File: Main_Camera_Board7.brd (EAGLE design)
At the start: 127 x 50.8 mm, 8 parts

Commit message: put leds in correct positions
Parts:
- moved U$3 15.2 mm to (111.8, 29.2)
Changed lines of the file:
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@@
 <?xml version="1.0" encoding="utf-8"?>
 <!DOCTYPE eagle SYSTEM "eagle.dtd">
-<eagle version="7.6.0">
+<eagle version="7.7.0">
 <drawing>
 <settings>
@@
 <setting verticaltext="up"/>
 </settings>
-<grid distance="0.05" unitdist="mm" unit="mm" style="lines" multiple="1" display="yes" altdistance="0.025" altunitdist="inch" altunit="inch"/>
+<grid distance="0.01" unitdist="inch" unit="inch" style="lines" multiple="1" display="yes" altdistance="0.025" altunitdist="inch" altunit="inch"/>
 <layers>
 <layer number="1" name="Top" color="4" fill="1" visible="yes" active="yes"/>
@@
 <element name="U$1" library="camera" package="ELP-USBFHD01M-L21" value="ELP-USBFHD01M-L21" x="58.42" y="25.4"/>
 <element name="U$2" library="camera" package="LED" value="LED" x="10.16" y="29.21"/>
-<element name="U$3" library="camera" package="LED" value="LED" x="96.52" y="29.21"/>
+<element name="U$3" library="camera" package="LED" value="LED" x="111.76" y="29.16"/>
 <element name="U$4" library="camera" package="T2I" value="T21" x="1.75" y="44.45" rot="R270"/>
 <element name="U$5" library="camera" package="T2I" value="T21" x="1.75" y="25.4" rot="R270"/>
@@
 <contactref element="U$3" pad="P$3"/>
 <contactref element="U$3" pad="P$1"/>
-<wire x1="96.52" y1="29.21" x2="97.67" y2="29.21" width="0" layer="19" extent="1-1"/>
-<wire x1="11.31" y1="29.21" x2="96.52" y2="29.21" width="0" layer="19" extent="1-1"/>
+<wire x1="111.76" y1="29.16" x2="112.91" y2="29.16" width="0" layer="19" extent="1-1"/>
+<wire x1="11.31" y1="29.21" x2="111.76" y2="29.16" width="0" layer="19" extent="1-1"/>
 <wire x1="10.16" y1="29.21" x2="11.31" y2="29.21" width="0" layer="19" extent="1-1"/>
 <wire x1="1.75" y1="37.05" x2="10.16" y2="29.21" width="0" layer="19" extent="1-1"/>

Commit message: more updates
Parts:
- moved SERVO 77.4 mm to (95.7, 3.08)
- moved U$3 15.2 mm to (96.5, 29.2)
- flipped LIGHT1 to the bottom
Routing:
- net PWN: track 0.00 -> 113.2 mm
- net +5VCAMERA: track 14.0 -> 110.5 mm
- net +3.3V: track 137.9 -> 50.2 mm
- net N$8: track 0.00 -> 86.2 mm
- net N$5: track 57.8 -> 0.00 mm
- net N$1: track 43.3 -> 0.00 mm
- net N$6: track 10.8 -> 0.00 mm
- net D_P: track 60.6 -> 58.9 mm
- net D_M: track 63.7 -> 62.6 mm

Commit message: Added TODO list
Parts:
- moved U$3 14.5 mm to (111.0, 29.2)
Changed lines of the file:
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@@
 <?xml version="1.0" encoding="utf-8"?>
 <!DOCTYPE eagle SYSTEM "eagle.dtd">
-<eagle version="7.6.0">
+<eagle version="7.7.0">
 <drawing>
 <settings>
@@
 <setting verticaltext="up"/>
 </settings>
-<grid distance="0.05" unitdist="mm" unit="mm" style="lines" multiple="1" display="yes" altdistance="0.025" altunitdist="inch" altunit="inch"/>
+<grid distance="0.01" unitdist="inch" unit="inch" style="lines" multiple="1" display="yes" altdistance="0.025" altunitdist="inch" altunit="inch"/>
 <layers>
 <layer number="1" name="Top" color="4" fill="1" visible="yes" active="yes"/>
@@
 <element name="U$1" library="camera" package="ELP-USBFHD01M-L21" value="ELP-USBFHD01M-L21" x="58.42" y="25.4"/>
 <element name="U$2" library="camera" package="LED" value="LED" x="10.16" y="29.21"/>
-<element name="U$3" library="camera" package="LED" value="LED" x="96.52" y="29.21"/>
+<element name="U$3" library="camera" package="LED" value="LED" x="110.998" y="29.21"/>
 <element name="U$4" library="camera" package="T2I" value="T21" x="1.75" y="44.45" rot="R270"/>
 <element name="U$5" library="camera" package="T2I" value="T21" x="1.75" y="25.4" rot="R270"/>
@@
 <contactref element="U$3" pad="P$3"/>
 <contactref element="U$3" pad="P$1"/>
-<wire x1="96.52" y1="29.21" x2="97.67" y2="29.21" width="0" layer="19" extent="1-1"/>
-<wire x1="11.31" y1="29.21" x2="96.52" y2="29.21" width="0" layer="19" extent="1-1"/>
+<wire x1="110.998" y1="29.21" x2="112.148" y2="29.21" width="0" layer="19" extent="1-1"/>
+<wire x1="11.31" y1="29.21" x2="110.998" y2="29.21" width="0" layer="19" extent="1-1"/>
 <wire x1="10.16" y1="29.21" x2="11.31" y2="29.21" width="0" layer="19" extent="1-1"/>
 <wire x1="1.75" y1="37.05" x2="10.16" y2="29.21" width="0" layer="19" extent="1-1"/>

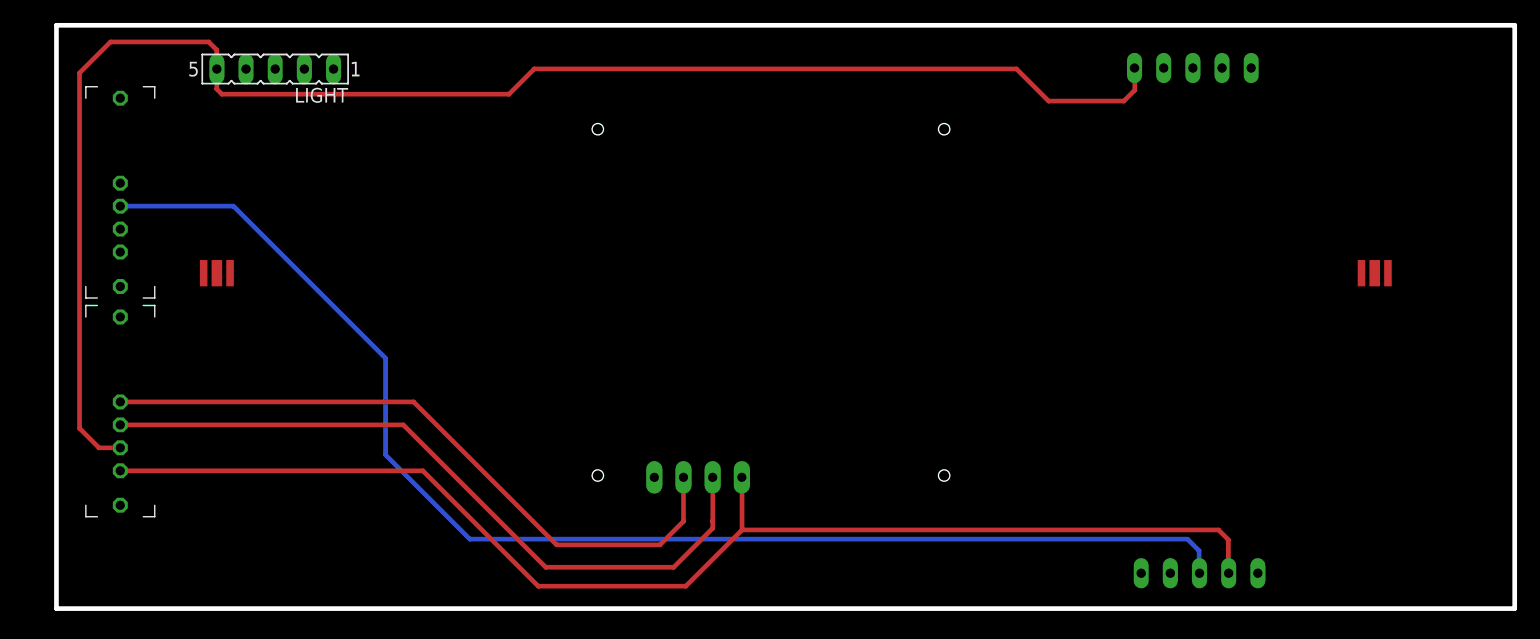
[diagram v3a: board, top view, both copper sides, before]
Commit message: made a few changes to camera board
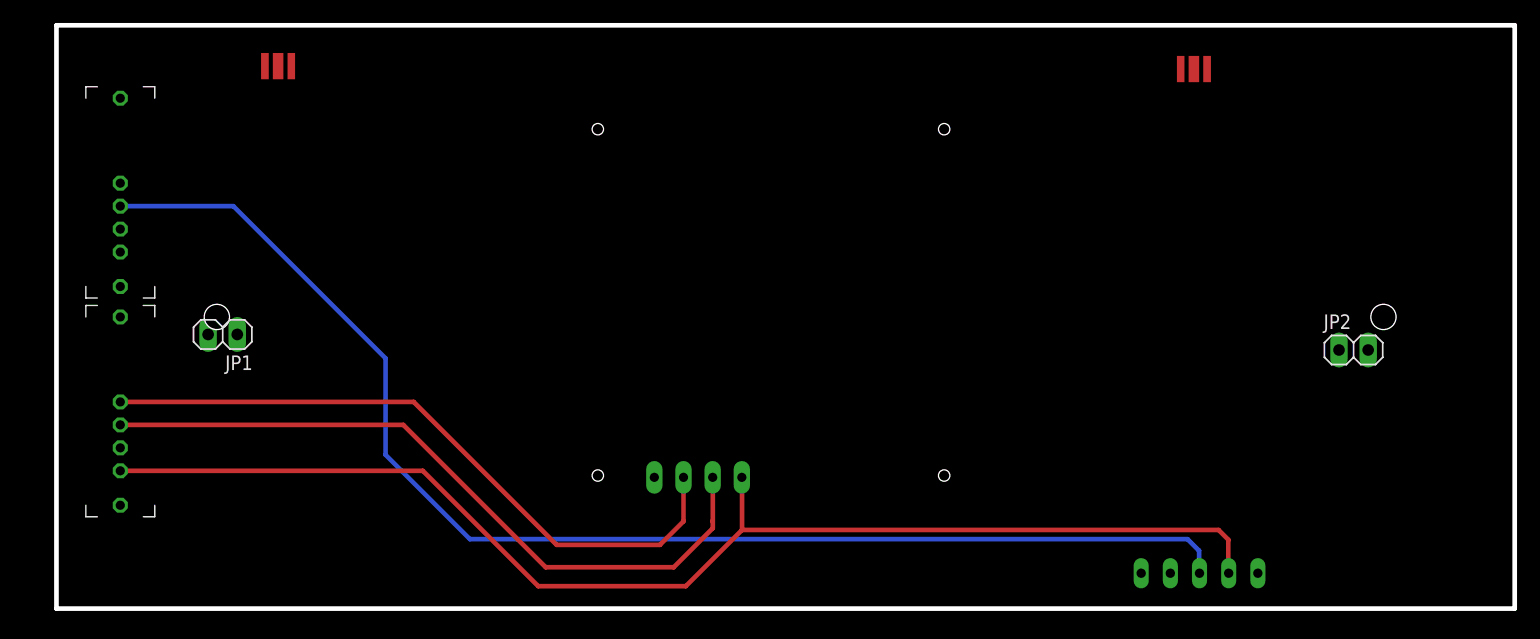
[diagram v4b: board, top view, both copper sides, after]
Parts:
- removed LIGHT, LIGHT1: (no value), con-lsta:FE05-1
- added JP1, JP2: (no value), pinhead:1X02
- moved U$3 23.8 mm to (95.2, 47.0)
- moved U$2 18.8 mm to (15.5, 47.2)
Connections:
- net +3.3V: no longer LIGHT.5, LIGHT1.5
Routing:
- net N$8: track 86.2 -> 0.00 mm
- net +3.3V: track 50.2 -> 0.00 mm
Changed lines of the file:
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@@
 <layers>
 <layer number="1" name="Top" color="4" fill="1" visible="yes" active="yes"/>
+<layer number="2" name="Route2" color="1" fill="3" visible="no" active="no"/>
+<layer number="3" name="Route3" color="4" fill="3" visible="no" active="no"/>
+<layer number="14" name="Route14" color="1" fill="6" visible="no" active="no"/>
+<layer number="15" name="Route15" color="4" fill="6" visible="no" active="no"/>
 <layer number="16" name="Bottom" color="1" fill="1" visible="yes" active="yes"/>
 <layer number="17" name="Pads" color="2" fill="1" visible="yes" active="yes"/>
@@
 <wire x1="109.22" y1="31.75" x2="109.22" y2="26.67" width="0.4064" layer="51"/>
 <text x="-5.08" y="53.34" size="1.778" layer="51">5 in x 2 in</text>
+<hole x="10.16" y="25.4" drill="2.2"/>
+<hole x="111.76" y="25.4" drill="2.2"/>
 </plain>
 <attributes>
@@
 <attribute name="OC_NEWARK" value="unknown" x="95.74" y="3.08" size="1.778" layer="28" rot="MR0" display="off"/>
 </element>
-<element name="LIGHT" library="con-lsta" package="FE05-1" value="" x="15.24" y="46.99" rot="R180">
-<attribute name="MF" value="" x="15.24" y="46.99" size="1.778" layer="27" rot="R180" display="off"/>
-<attribute name="OC_FARNELL" value="unknown" x="15.24" y="46.99" size="1.778" layer="27" rot="R180" display="off"/>
-<attribute name="MPN" value="" x="15.24" y="46.99" size="1.778" layer="27" rot="R180" display="off"/>
-<attribute name="OC_NEWARK" value="unknown" x="15.24" y="46.99" size="1.778" layer="27" rot="R180" display="off"/>
-</element>
-<element name="LIGHT1" library="con-lsta" package="FE05-1" value="" x="95.16" y="47.08" rot="MR0">
-<attribute name="MPN" value="" x="95.16" y="47.08" size="1.778" layer="28" rot="MR0" display="off"/>
-<attribute name="OC_FARNELL" value="unknown" x="95.16" y="47.08" size="1.778" layer="28" rot="MR0" display="off"/>
-<attribute name="OC_NEWARK" value="unknown" x="95.16" y="47.08" size="1.778" layer="28" rot="MR0" display="off"/>
-<attribute name="MF" value="" x="95.16" y="47.08" size="1.778" layer="28" rot="MR0" display="off"/>
-</element>
 <element name="U$1" library="camera" package="ELP-USBFHD01M-L21" value="ELP-USBFHD01M-L21" x="58.42" y="25.4"/>
-<element name="U$2" library="camera" package="LED" value="LED" x="10.16" y="29.21"/>
-<element name="U$3" library="camera" package="LED" value="LED" x="110.998" y="29.21"/>
+<element name="U$2" library="camera" package="LED" value="LED" x="15.494" y="47.244"/>
+<element name="U$3" library="camera" package="LED" value="LED" x="95.25" y="46.99"/>
 <element name="U$4" library="camera" package="T2I" value="T21" x="1.75" y="44.45" rot="R270"/>
 <element name="U$5" library="camera" package="T2I" value="T21" x="1.75" y="25.4" rot="R270"/>
+<element name="JP1" library="pinhead" package="1X02" value="" x="10.668" y="23.876" rot="R180"/>
+<element name="JP2" library="pinhead" package="1X02" value="" x="109.158" y="22.522"/>
 </elements>
 <signals>
@@
 <contactref element="U$3" pad="P$3"/>
 <contactref element="U$3" pad="P$1"/>
-<wire x1="110.998" y1="29.21" x2="112.148" y2="29.21" width="0" layer="19" extent="1-1"/>
-<wire x1="11.31" y1="29.21" x2="110.998" y2="29.21" width="0" layer="19" extent="1-1"/>
-<wire x1="10.16" y1="29.21" x2="11.31" y2="29.21" width="0" layer="19" extent="1-1"/>
-<wire x1="1.75" y1="37.05" x2="10.16" y2="29.21" width="0" layer="19" extent="1-1"/>
+<wire x1="95.25" y1="46.99" x2="96.4" y2="46.99" width="0" layer="19" extent="1-1"/>
+<wire x1="16.644" y1="47.244" x2="95.25" y2="46.99" width="0" layer="19" extent="1-1"/>
+<wire x1="15.494" y1="47.244" x2="16.644" y2="47.244" width="0" layer="19" extent="1-1"/>
+<wire x1="1.75" y1="37.05" x2="15.494" y2="47.244" width="0" layer="19" extent="1-1"/>
 </signal>
 <signal name="+3.3V">
-<contactref element="LIGHT" pad="5"/>
-<contactref element="LIGHT1" pad="5"/>
 <contactref element="U$5" pad="P$4"/>
-<wire x1="1.75" y1="14" x2="-0.1" y2="14" width="0.4064" layer="1"/>
-<wire x1="-0.1" y1="14" x2="-1.8" y2="15.7" width="0.4064" layer="1"/>
-<wire x1="-1.8" y1="15.7" x2="-1.8" y2="46.65" width="0.4064" layer="1"/>
-<wire x1="-1.8" y1="46.65" x2="0.9" y2="49.35" width="0.4064" layer="1"/>
-<wire x1="0.9" y1="49.35" x2="9.45" y2="49.35" width="0.4064" layer="1"/>
-<wire x1="9.45" y1="49.35" x2="10.15" y2="48.65" width="0.4064" layer="1"/>
-<wire x1="10.15" y1="48.65" x2="10.15" y2="47.05" width="0.4064" layer="1"/>
-<wire x1="10.16" y1="46.99" x2="90.08" y2="47.08" width="0" layer="19" extent="1-1"/>
-<wire x1="10.15" y1="47.05" x2="10.16" y2="46.99" width="0" layer="19" extent="1-1"/>
 </signal>
 <signal name="D_M">
@@
 </signal>
 <signal name="N$8">
-<wire x1="10.15" y1="47" x2="10.15" y2="45.25" width="0.4064" layer="1"/>
-<wire x1="10.15" y1="45.25" x2="10.6" y2="44.8" width="0.4064" layer="1"/>
-<wire x1="10.6" y1="44.8" x2="35.6" y2="44.8" width="0.4064" layer="1"/>
-<wire x1="35.6" y1="44.8" x2="37.8" y2="47" width="0.4064" layer="1"/>
-<wire x1="37.8" y1="47" x2="79.8" y2="47" width="0.4064" layer="1"/>
-<wire x1="79.8" y1="47" x2="82.6" y2="44.2" width="0.4064" layer="1"/>
-<wire x1="82.6" y1="44.2" x2="89.15" y2="44.2" width="0.4064" layer="1"/>
-<wire x1="89.15" y1="44.2" x2="90.1" y2="45.15" width="0.4064" layer="1"/>
-<wire x1="90.1" y1="45.15" x2="90.1" y2="47" width="0.4064" layer="1"/>
 </signal>
 </signals>

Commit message: Fixed schematic errors
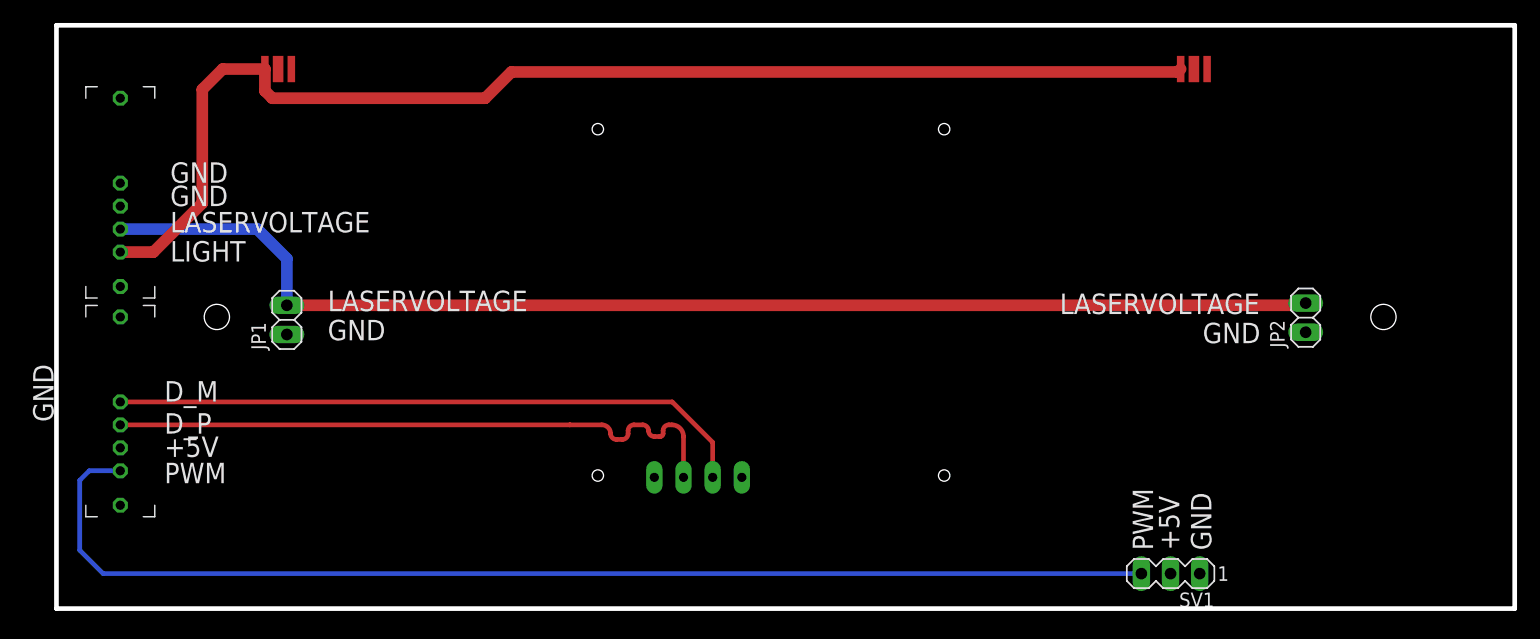
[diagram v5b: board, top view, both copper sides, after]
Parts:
- removed SERVO: (no value), con-lsta:FE05-1
- added SV1: (no value), con-lstb:MA03-1
- moved JP1 5.73 mm to (16.3, 25.1), turned to 90 degrees
- moved JP2 5.03 mm to (105.0, 25.3), turned to 90 degrees
- moved U$2 0.25 mm to (15.5, 47.0)
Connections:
- removed net +3.3V: U$5.P$4
- removed net +5VCAMERA: SERVO.2, U$1.P$1, U$5.P$5
- removed net PWN: SERVO.3, U$4.P$3
- new net LASER: JP1.2, JP2.2, U$4.P$4
- new net LIGHT: U$2.P$2, U$3.P$2, U$4.P$5
- new net PWM: SV1.3, U$5.P$5
- net +5V: now also SV1.2, U$1.P$1, U$5.P$4; no longer U$2.P$1, U$2.P$3, U$3.P$1, U$3.P$3, U$4.P$2
- net D_M: now also U$5.P$2; no longer U$5.P$3
- net D_P: now also U$5.P$3; no longer U$5.P$2
- net GND: now also JP1.1, JP2.1, SV1.1, U$2.P$1, U$2.P$3, U$3.P$1, U$3.P$3, U$4.P$2, U$4.P$3; no longer SERVO.1, U$4.P$4, U$4.P$5
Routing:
- net PWN: track 113.2 -> 0.00 mm
- net +5VCAMERA: track 110.5 -> 0.00 mm
- net LASER: track 0.00 -> 108.4 mm
- net LIGHT: track 0.00 -> 108.0 mm
- net PWM: track 0.00 -> 103.3 mm
- net D_M: track 62.6 -> 56.1 mm
- net D_P: track 58.9 -> 55.2 mm
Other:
- board text added: "+5V"
- board text added: "D_M"
- board text added: "D_P"
- board text added: "GND"
- board text added: "LASERVOLTAGE"
- board text added: "LIGHT"
- board text added: "PWM"
